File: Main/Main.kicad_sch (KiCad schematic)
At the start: 67 parts, among them J1 Conn_02x16_Odd_Even, J2 TYPE-C 6P, Q3 S9013 J3(RANGE:200-350), SW2 SS-12D11G3R, U1 BQ24074RGT, U2 DRV8833PW, U3 HUSB237-AA001-DN06R, U4 RT9742GGJ5, U5 RT9742GGJ5, U6 INA219AxDCN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

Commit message: Did some error fixing
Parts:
- added TP12, TP13, TP14, TP15, TP16, TP17, TP18, TP19: TestPoint, TestPoint:TestPoint_Pad_D3.0mm, symbol Connector:TestPoint
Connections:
- net GND: now also TP12.1, TP14.1, TP17.1, TP19.1
- net at R1.1, U3.3 (VSET): now also TP15.1
- net at R9.1, U1.12 (ILIM): now also TP18.1
- net at Q3.2 (E), R11.1: now also TP16.1

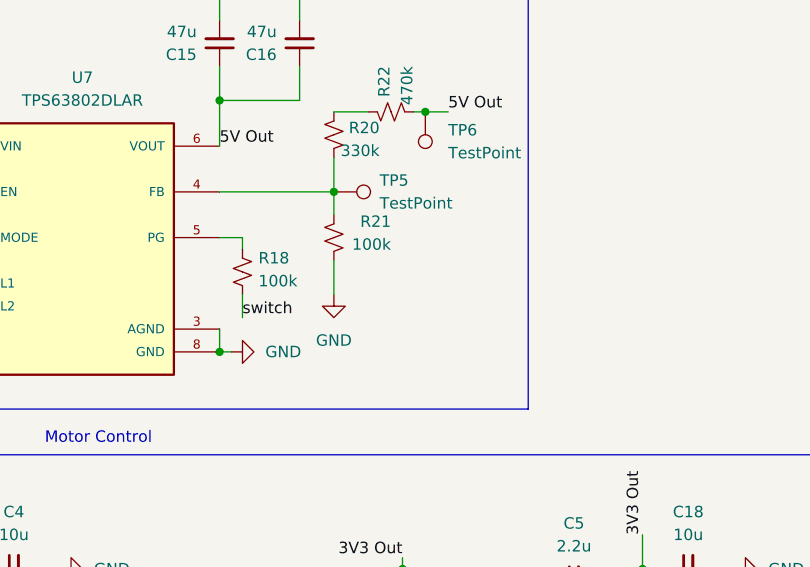
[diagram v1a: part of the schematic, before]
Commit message: Corrected LCSC of parts
Initially accidentally labelled the LCSC of components as (LSCS) which generated an error. This version fixed these issues.
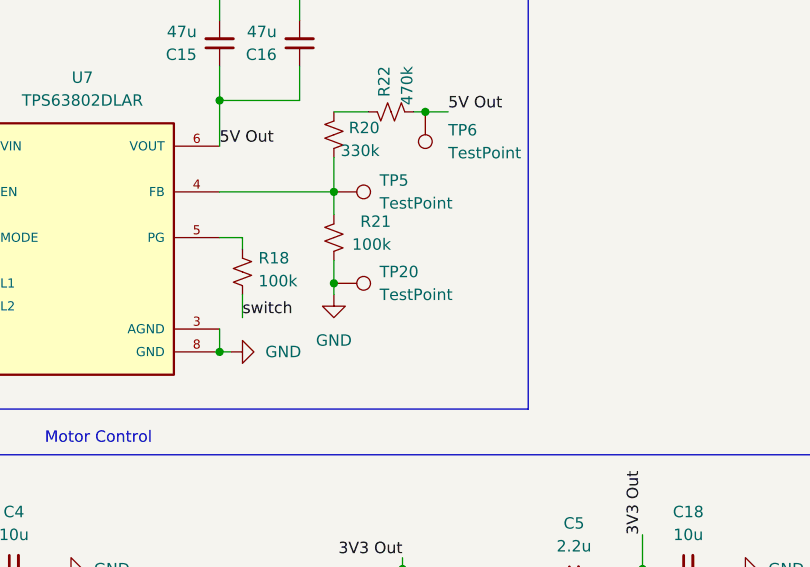
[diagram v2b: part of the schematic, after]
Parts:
- added TP20: TestPoint, TestPoint:TestPoint_Pad_D3.0mm, symbol Connector:TestPoint
- C12, C13: LCSC (none) -> C45783; LSCS C45783 -> (none)
- C15, C16: LCSC (none) -> C96123; LSCS C96123 -> (none)
- C17, C19: LCSC (none) -> C19702; LSCS C19702 -> (none)
- C18, C4: LCSC (none) -> C15525; LSCS C15525 -> (none)
- C2, C5: LCSC (none) -> C12530; LSCS C12530 -> (none)
- C3, C6: LCSC (none) -> C1710; LSCS C1710 -> (none)
- R17, R5, R6: LCSC (none) -> C247521; LSCS C247521 -> (none)
- R18, R21: LCSC (none) -> C25741; LSCS C25741 -> (none)
- R19, R4: LCSC (none) -> C17414; LSCS C17414 -> (none)
- R20: LCSC (none) -> C23137; LSCS C23137 -> (none)
- R22: LCSC (none) -> C23178; LSCS C23178 -> (none)
- R23: LCSC (none) -> C25744; LSCS C25744 -> (none)
- R3: LCSC (none) -> C17928; LSCS C17928 -> (none)
- U2, U8: LCSC (none) -> C50506; LSCS C50506 -> (none)
- U9: LCSC (none) -> C6186; LSCS C6186 -> (none)
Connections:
- net GND: now also TP20.1
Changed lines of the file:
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@@
 	)
 	(junction
+		(at 207.01 109.22)
+		(diameter 0)
+		(color 0 0 0 0)
+	)
+	(junction
 		(at 217.17 232.41)
 		(diameter 0)
@@
 	(wire
 		(pts
-			(xy 207.01 106.68) (xy 207.01 110.49)
+			(xy 207.01 106.68) (xy 207.01 109.22)
 		)
 		(stroke
@@
 	(wire
 		(pts
+			(xy 207.01 109.22) (xy 207.01 110.49)
+		)
+		(stroke
+			(width 0)
+			(type default)
+		)
+	)
+	(wire
+		(pts
 			(xy 181.61 24.13) (xy 181.61 36.83)
 		)
@@
 			)
 		)
-		(property "LSCS" "C247521"
+		(property "LCSC" "C247521"
 			(at 144.78 226.06 90)
 			(effects
@@
 			)
 		)
-		(property "LSCS" "C96123"
+		(property "LCSC" "C96123"
 			(at 203.2 82.55 0)
 			(effects
@@
 			)
 		)
-		(property "LSCS" "C25741"
+		(property "LCSC" "C25741"
 			(at 207.01 104.14 0)
 			(effects
@@
 			)
 		)
-		(property "LSCS" "C12530"
+		(property "LCSC" "C12530"
 			(at 233.68 142.24 90)
 			(effects
@@
 			)
 		)
-		(property "LSCS" "C45783"
+		(property "LCSC" "C45783"
 			(at 151.13 91.44 90)
 			(effects
@@
 			)
 		)
-		(property "LSCS" "C19702"
+		(property "LCSC" "C19702"
 			(at 238.76 237.49 0)
 			(effects
@@
 			)
 		)
-		(property "LSCS" "C17414"
+		(property "LCSC" "C17414"
 			(at 217.17 147.32 0)
 			(effects
@@
 			)
 		)
-		(property "LSCS" " C50506"
+		(property "LCSC" " C50506"
 			(at 233.68 162.56 0)
 			(effects
@@
 			)
 		)
-		(property "LSCS" "C15525"
+		(property "LCSC" "C15525"
 			(at 171.45 140.97 90)
 			(effects
@@
 			)
 		)
-		(property "LSCS" " C50506"
+		(property "LCSC" " C50506"
 			(at 158.75 162.56 0)
 			(effects
@@
 			)
 		)
-		(property "LSCS" "C23178"
+		(property "LCSC" "C23178"
 			(at 213.36 90.17 0)
 			(effects
@@
 			)
 		)
-		(property "LSCS" "C12530"
+		(property "LCSC" "C12530"
 			(at 158.75 142.24 90)
 			(effects
@@
 			)
 		)
-		(property "LSCS" "C1710"
+		(property "LCSC" "C1710"
 			(at 213.36 152.4 0)
 			(effects
@@
 			)
 		)
-		(property "LSCS" "C45783"
+		(property "LCSC" "C45783"
 			(at 151.13 96.52 90)
 			(effects
@@
 			)
 		)
-		(property "LSCS" "C17928"
+		(property "LCSC" "C17928"
 			(at 125.73 167.64 90)
 			(effects
@@
 			)
 		)
-		(property "LSCS" "C19702"
+		(property "LCSC" "C19702"
 			(at 217.17 237.49 0)
 			(effects
@@
 			)
 		)
-		(property "LSCS" "C247521"
+		(property "LCSC" "C247521"
 			(at 137.16 226.06 90)
 			(effects
@@
 			)
 		)
-		(property "LSCS" "C17414"
+		(property "LCSC" "C17414"
 			(at 142.24 147.32 0)
 			(effects
@@
 			)
 		)
-		(property "LSCS" "C96123"
+		(property "LCSC" "C96123"
 			(at 194.31 82.55 0)
 			(effects
@@
 			)
 		)
-		(property "LSCS" "C25744"
+		(property "LCSC" "C25744"
 			(at 232.41 205.74 90)
 			(effects
@@
 			)
 		)
-		(property "LSCS" "C1710"
+		(property "LCSC" "C1710"
 			(at 138.43 152.4 0)
 			(effects
@@
 			)
 		)
-		(property "LSCS" "C15525"
+		(property "LCSC" "C15525"
 			(at 246.38 140.97 90)
 			(effects
@@
 			)
 		)
-		(property "LSCS" "C25741"
+		(property "LCSC" "C25741"
 			(at 196.85 107.95 0)
 			(effects
@@
 	)
 	(symbol
+		(lib_id "Connector:TestPoint")
+		(at 207.01 109.22 270)
+		(unit 1)
+		(exclude_from_sim no)
+		(in_bom yes)
+		(on_board yes)
+		(dnp no)
+		(fields_autoplaced yes)
+		(property "Reference" "TP20"
+			(at 212.09 107.9499 90)
+			(effects
+				(font
+					(size 1.27 1.27)
+				)
+				(justify left)
+			)
+		)
+		(property "Value" "TestPoint"
+			(at 212.09 110.4899 90)
+			(effects
+				(font
+					(size 1.27 1.27)
+				)
+				(justify left)
+			)
+		)
+		(property "Footprint" "TestPoint:TestPoint_Pad_D3.0mm"
+			(at 207.01 114.3 0)
+			(effects
+				(font
+					(size 1.27 1.27)
+				)
+				(hide yes)
+			)
+		)
+		(property "Datasheet" "~"
+			(at 207.01 114.3 0)
+			(effects
+				(font
+					(size 1.27 1.27)
+				)
+				(hide yes)
+			)
+		)
+		(property "Description" "test point"
+			(at 207.01 109.22 0)
+			(effects
+				(font
+					(size 1.27 1.27)
+				)
+				(hide yes)
+			)
+		)
+		(pin "1"
+		)
+		(instances
+			(project "Main"
+				(path "/0f55449c-8e79-4f10-a328-a1bcb934c334"
+					(reference "TP20")
+					(unit 1)
+				)
+			)
+		)
+	)
+	(symbol
 		(lib_id "power:GND")
 		(at 203.2 77.47 180)
@@
 			)
 		)
-		(property "LSCS" "C247521"
+		(property "LCSC" "C247521"
 			(at 200.66 167.64 90)
 			(effects
@@
 			)
 		)
-		(property "LSCS" "C23137"
+		(property "LCSC" "C23137"
 			(at 207.01 92.71 0)
 			(effects
@@
 			)
 		)
-		(property "LSCS" "C6186"
+		(property "LCSC" "C6186"
 			(at 228.6 232.41 0)
 			(effects

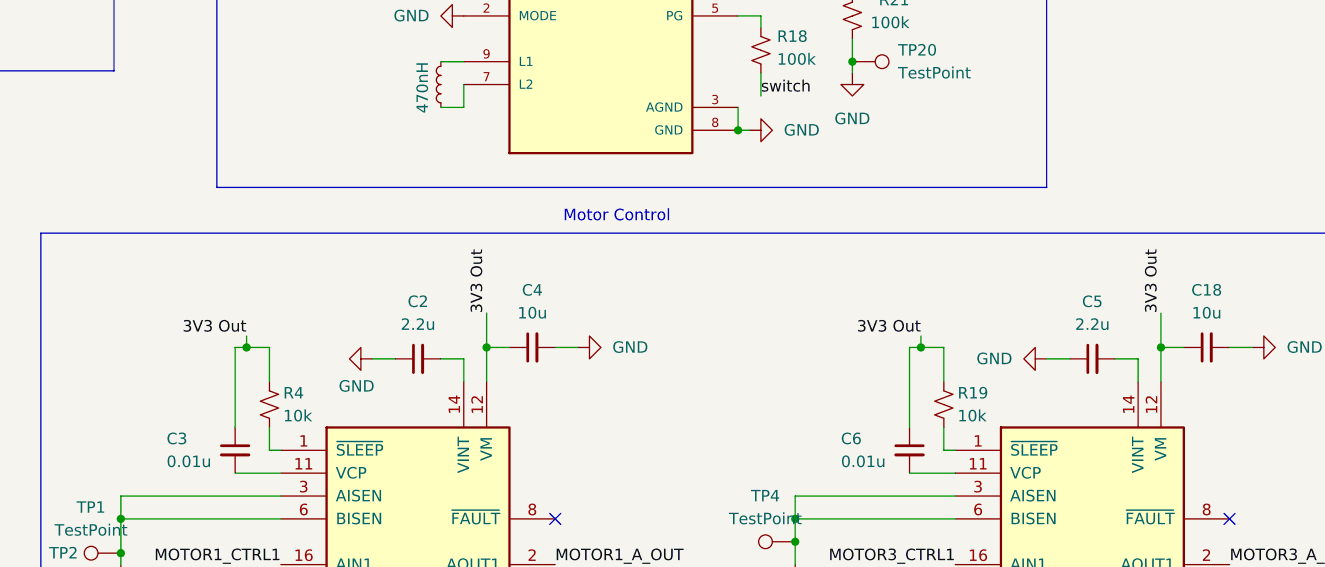
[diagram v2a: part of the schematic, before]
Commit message: Changed maximum motor voltage
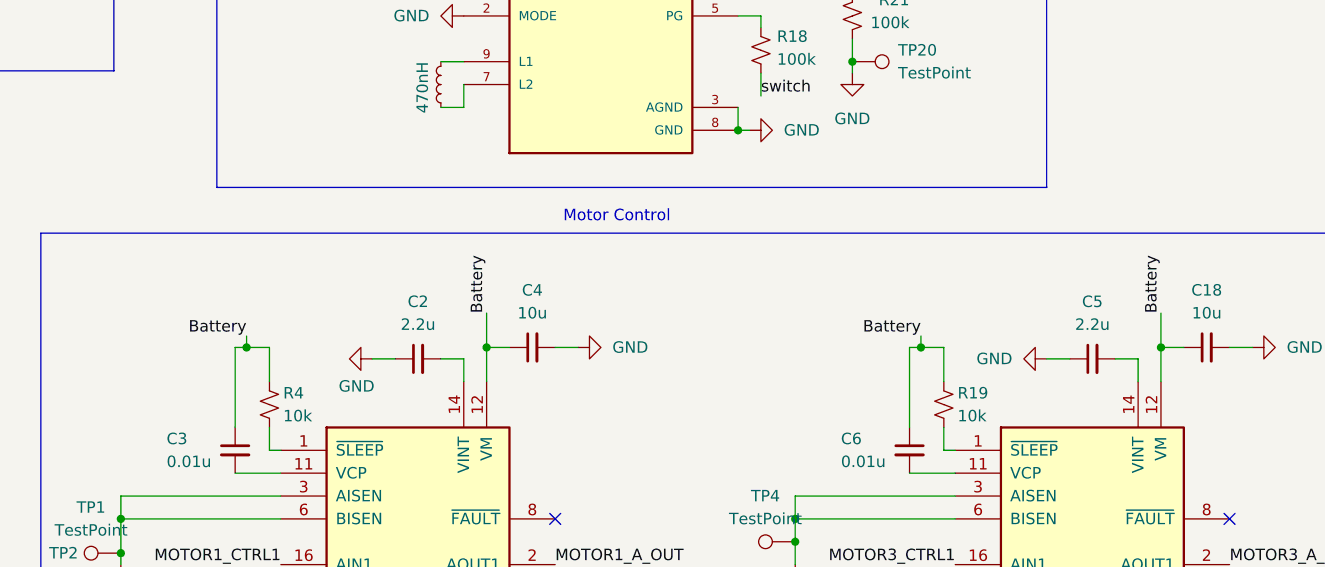
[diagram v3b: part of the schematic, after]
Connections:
- net 3V3 Out: no longer C18.1, C3.1, C4.1, C6.1, R19.1, R4.1, U2.12 (VM), U8.12 (VM)
- net Battery: now also C18.1, C3.1, C4.1, C6.1, R19.1, R4.1, U2.12 (VM), U8.12 (VM)
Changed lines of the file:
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@@
-		)
-	)
-	(label "3V3 Out"
-		(at 166.37 137.16 90)
-		(effects
-			(font
-				(size 1.27 1.27)
-			)
-			(justify left bottom)
 		)
 	)
@@
 		)
 	)
+	(label "Battery"
+		(at 139.7 139.7 180)
+		(effects
+			(font
+				(size 1.27 1.27)
+			)
+			(justify right bottom)
+		)
+	)
 	(label "High Voltage (9V)"
 		(at 190.5 41.91 180)
@@
 		)
 	)
+	(label "Battery"
+		(at 214.63 139.7 180)
+		(effects
+			(font
+				(size 1.27 1.27)
+			)
+			(justify right bottom)
+		)
+	)
 	(label "Motor2_B_OUT"
 		(at 364.49 30.48 0)
@@
 		)
 	)
-	(label "3V3 Out"
-		(at 241.3 137.16 90)
-		(effects
-			(font
-				(size 1.27 1.27)
-			)
-			(justify left bottom)
-		)
-	)
 	(label "I2C1_SDA"
 		(at 364.49 50.8 0)
@@
 		)
 	)
+	(label "Battery"
+		(at 241.3 137.16 90)
+		(effects
+			(font
+				(size 1.27 1.27)
+			)
+			(justify left bottom)
+		)
+	)
 	(label "3V3 Out"
 		(at 351.79 50.8 180)
@@
 		)
 	)
+	(label "Battery"
+		(at 166.37 137.16 90)
+		(effects
+			(font
+				(size 1.27 1.27)
+			)
+			(justify left bottom)
+		)
+	)
 	(label "MOTOR1_CTRL1"
 		(at 351.79 63.5 180)
@@
 		)
 	)
-	(label "3V3 Out"
-		(at 139.7 139.7 180)
-		(effects
-			(font
-				(size 1.27 1.27)
-			)
-			(justify right bottom)
-		)
-	)
 	(label "High Voltage (9V)"
 		(at 144.78 41.91 180)
@@
 		)
 	)
-	(label "3V3 Out"
-		(at 214.63 139.7 180)
-		(effects
-			(font
-				(size 1.27 1.27)
-			)
-			(justify right bottom)
-		)
-	)

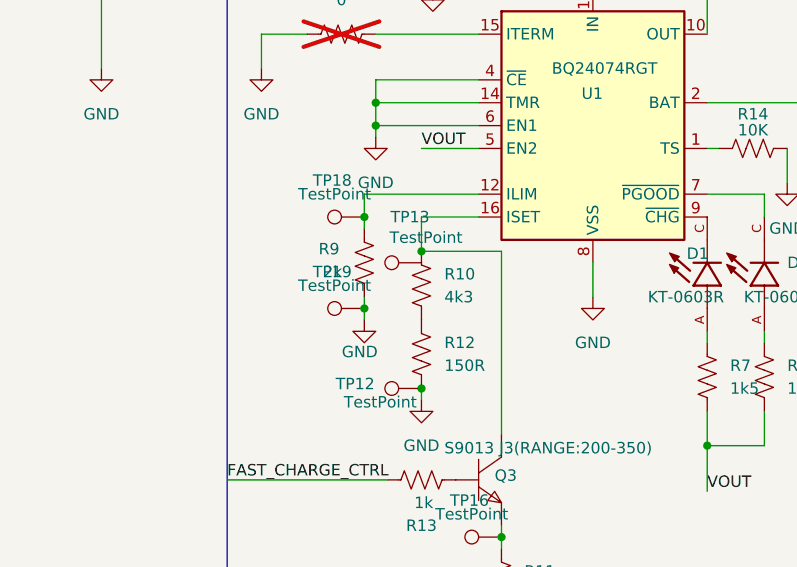
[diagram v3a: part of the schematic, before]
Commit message: Completed substantial PCB Connections
Completed: 1A Switching, Charging IC
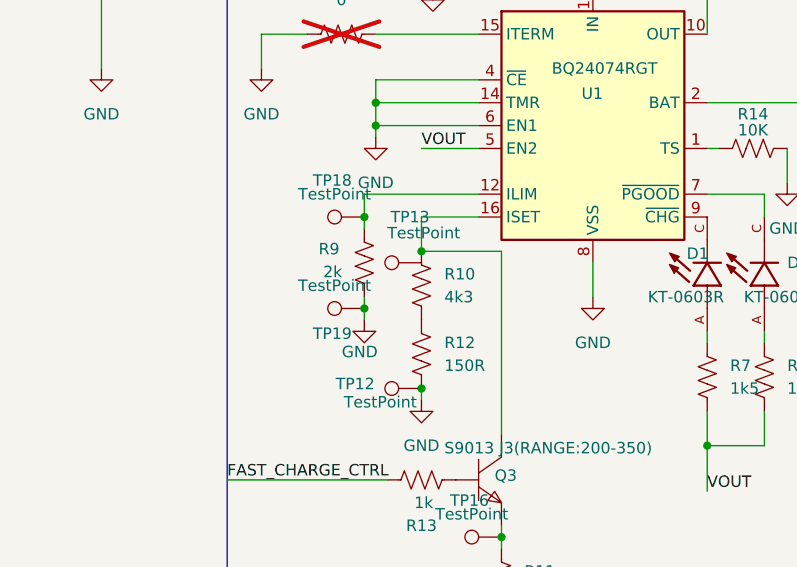
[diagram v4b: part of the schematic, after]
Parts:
- Q3: JCLC C6749 -> (none); LCSC (none) -> C6749
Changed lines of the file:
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@@
 		(dnp no)
 		(property "Reference" "TP19"
-			(at 57.404 59.436 90)
+			(at 57.404 66.294 90)
 			(effects
 				(font
@@
 		)
 		(property "Value" "TestPoint"
-			(at 67.818 55.626 90)
+			(at 67.564 55.118 90)
 			(effects
 				(font
@@
 			)
 		)
-		(property "JCLC" "C6749"
-			(at 73.66 82.55 0)
-			(effects
+		(property "LCSC" "C6749"
+			(at 73.66 82.55 0)
+			(effects

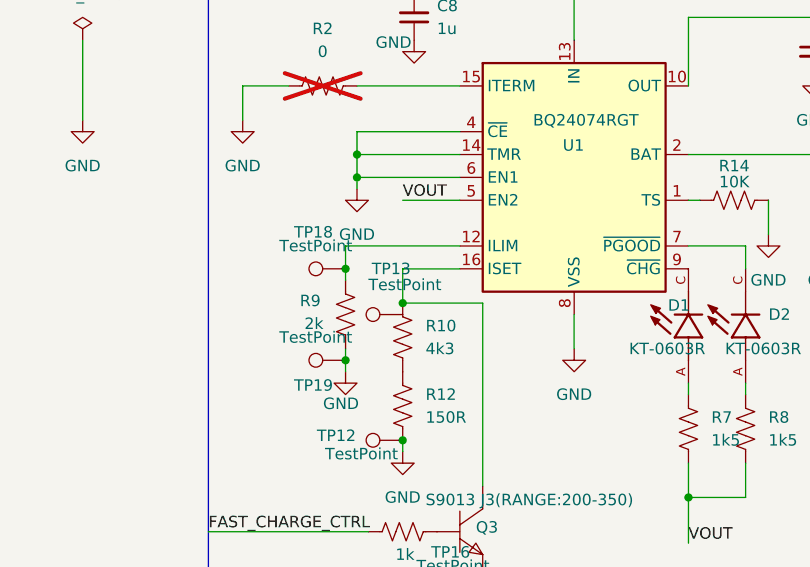
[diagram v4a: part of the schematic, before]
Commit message: PB-13 was unconnected - it is now connected
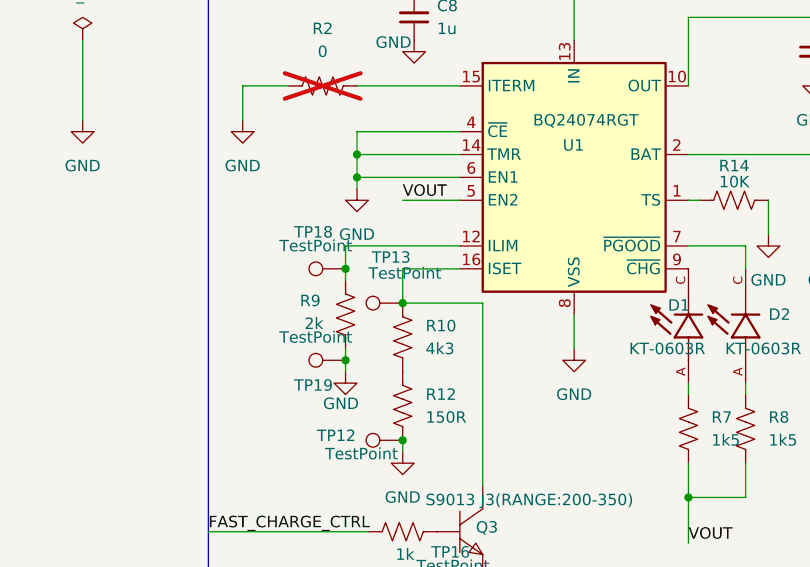
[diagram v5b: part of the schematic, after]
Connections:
- net at Q3.3 (C), R10.1, U1.16 (ISET): now also TP13.1
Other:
- moved on the sheet: TP13
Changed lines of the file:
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@@
 	(symbol
 		(lib_id "Connector:TestPoint")
-		(at 67.31 58.42 90)
+		(at 67.31 57.15 90)
 		(unit 1)
 		(exclude_from_sim no)
@@
 		(dnp no)
 		(property "Reference" "TP13"
-			(at 66.04 53.34 90)
+			(at 66.04 52.07 90)
 			(effects
 				(font
@@
 		)
 		(property "Value" "TestPoint"
-			(at 67.564 55.118 90)
+			(at 67.564 53.848 90)
 			(effects
 				(font
@@
 		)
 		(property "Footprint" "TestPoint:TestPoint_Pad_D3.0mm"
-			(at 67.31 53.34 0)
+			(at 67.31 52.07 0)
 			(effects
 				(font
@@
 		)
 		(property "Datasheet" "~"
-			(at 67.31 53.34 0)
+			(at 67.31 52.07 0)
 			(effects
 				(font
@@
 		)
 		(property "Description" "test point"
-			(at 67.31 58.42 0)
+			(at 67.31 57.15 0)
 			(effects
 				(font
